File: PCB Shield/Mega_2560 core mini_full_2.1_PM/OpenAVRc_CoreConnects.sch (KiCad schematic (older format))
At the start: 19 parts, among them P1 2560-core, P10 RX1TX1, P16 LCD, P6 Micro_sd, P9 SPI, Q1 IRLML5203

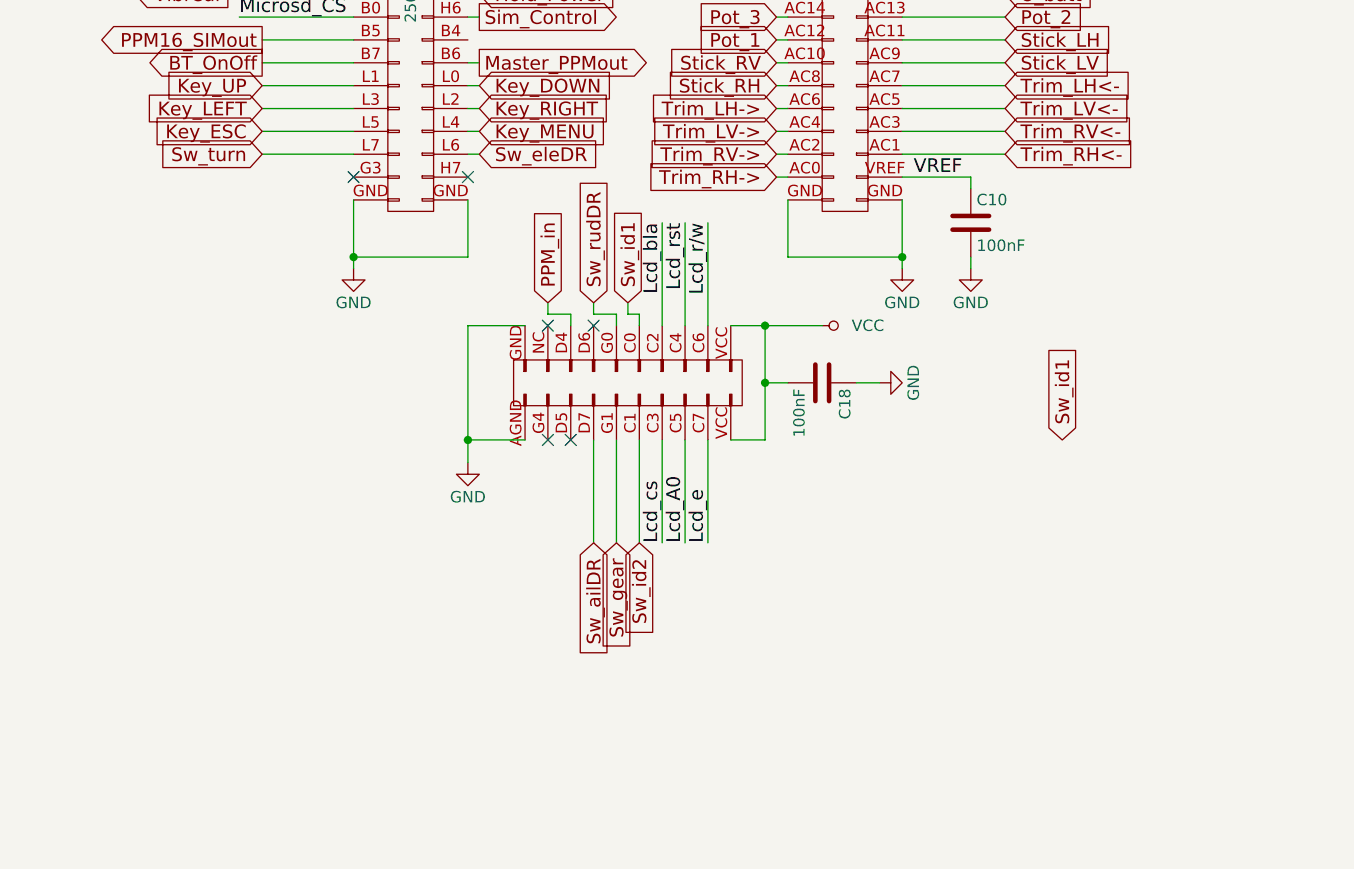
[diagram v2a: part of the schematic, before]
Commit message: Update schematic & pcb files
-remove P27.
-clean hold_power signal.
-add G3,H7 and G4 pins as dummy pins on 3 pins connector.
-update schematic.
-remove package errors in pcbnew.
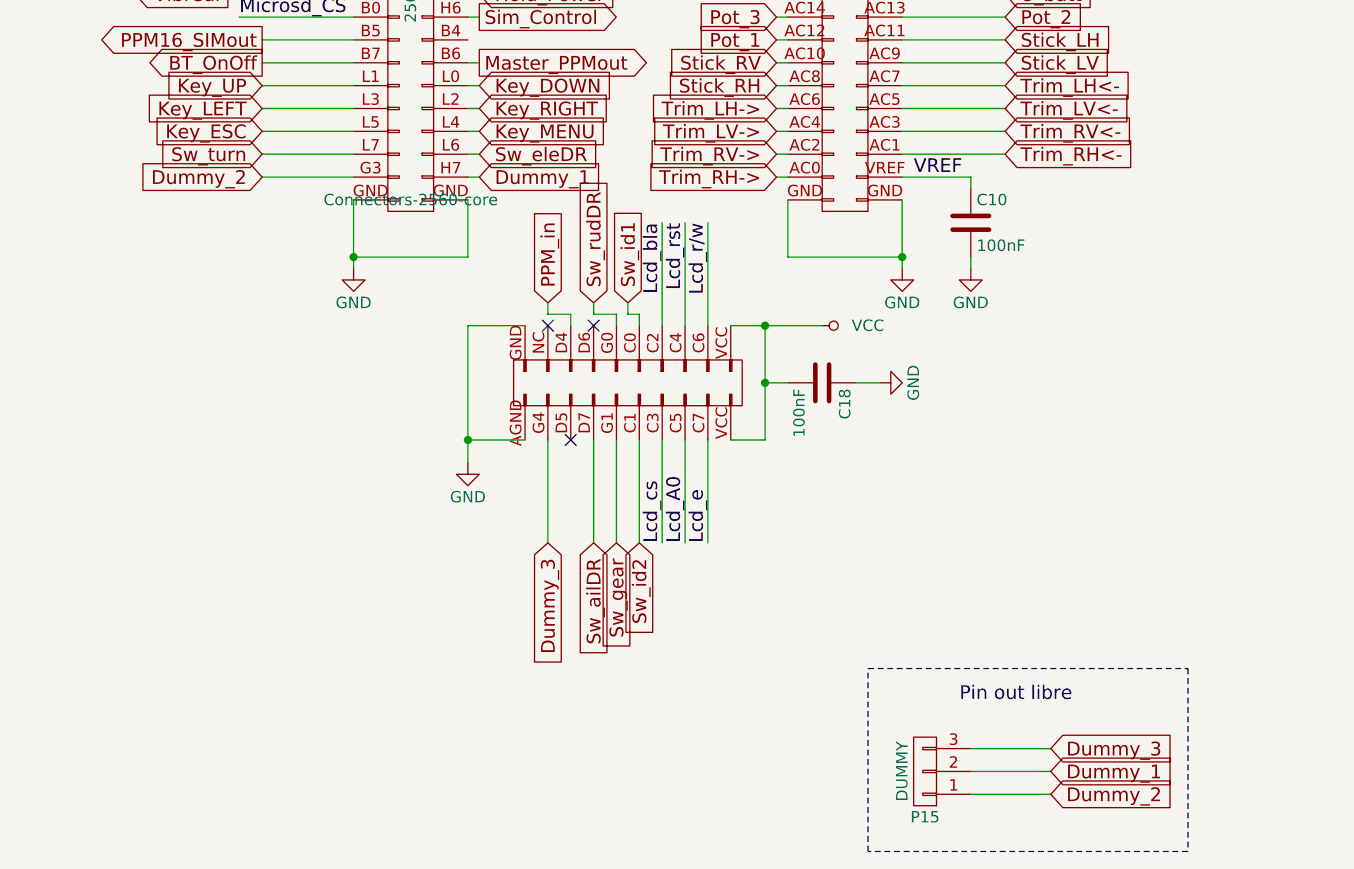
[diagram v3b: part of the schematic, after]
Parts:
- added P15: DUMMY, symbol CONN_01X03
- P1: footprint (none) -> Connectors-2560-core
- Q1: footprint (none) -> SOT-23_MOS_P
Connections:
- net Dummy_2: now reaches P1.G3 (P38)
- net Dummy_2: now also P15.1 (P1)
- net Dummy_3: now reaches P1.G4 (P97)
- net Dummy_3: now also P15.3 (P3)
- net Dummy_1: now reaches P1.H7 (P37)
- net Dummy_1: now also P15.2 (P2)
- no-connect marks 7 -> 4
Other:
- note added: "Pin out libre"

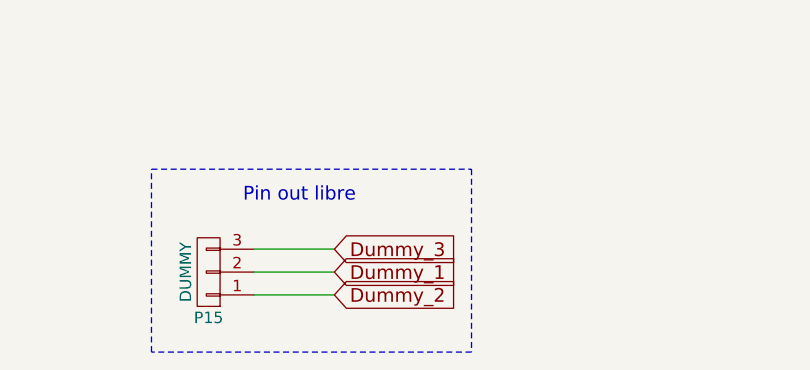
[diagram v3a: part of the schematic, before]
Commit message: Update schematic & pcb files
add mosfet function
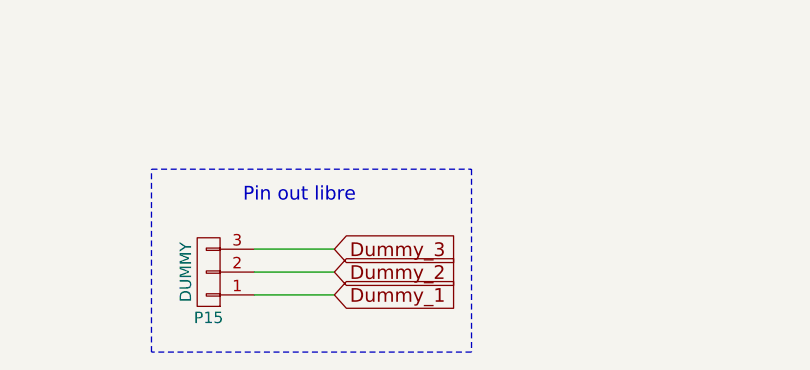
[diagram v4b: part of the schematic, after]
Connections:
- net Dummy_1: now also P15.1 (P1); no longer P15.2 (P2)
- net Dummy_2: now also P15.2 (P2); no longer P15.1 (P1)
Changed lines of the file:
@@
 Sheet 3 7
 Title "Shield Mega2560 core Full"
-Date "2018-03-06"
+Date "2018-03-16"
 Rev "2.10"
 Comp "© Team OpenAVRc"
@@
 	2700 5650 2700 5200
 Text GLabel 4900 6650 2    60   Input ~ 0
+Dummy_2
+Text GLabel 4900 6750 2    60   Input ~ 0
 Dummy_1
-Text GLabel 4900 6750 2    60   Input ~ 0
-Dummy_2
 Text GLabel 4900 6550 2    60   Input ~ 0
 Dummy_3

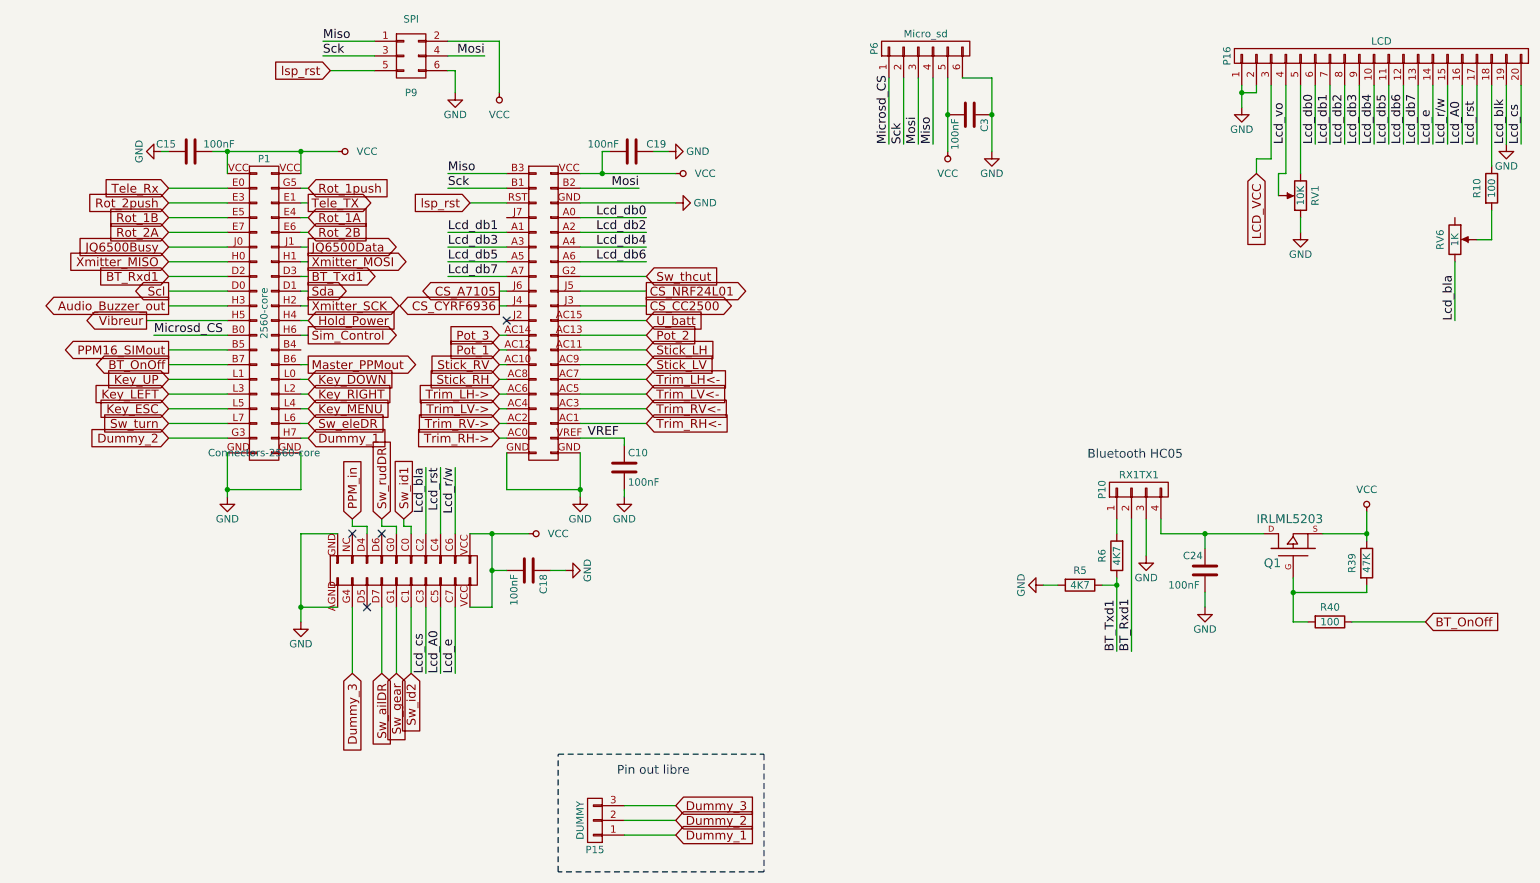
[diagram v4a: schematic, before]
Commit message: Udpade shild v2.1
remove c10 on VREF and R21,R38 on I2C
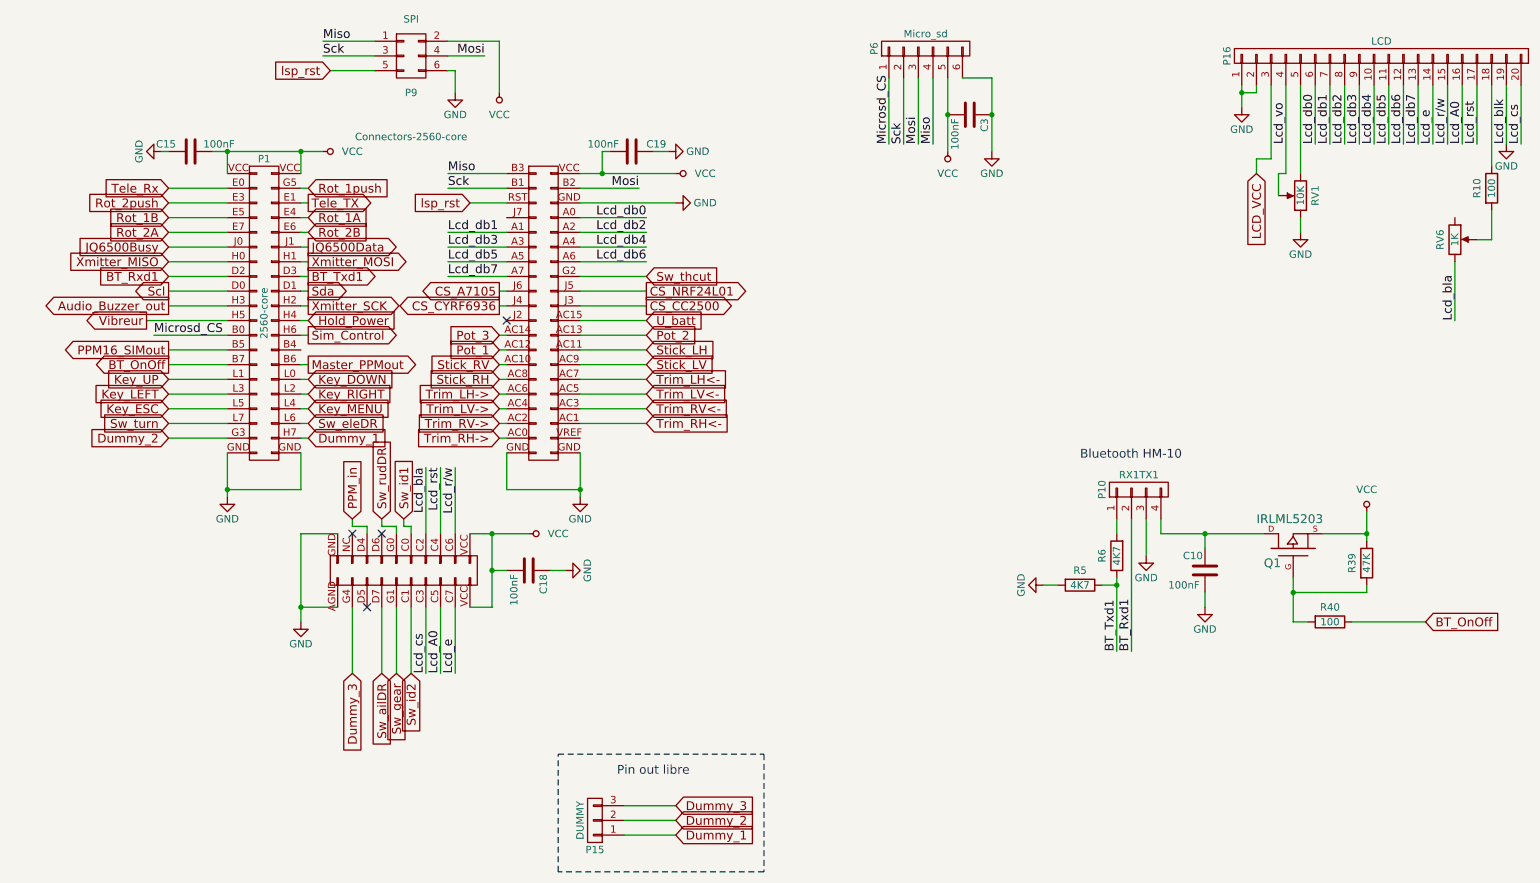
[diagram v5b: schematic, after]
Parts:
- removed C10: 100nF, Capacitors_SMD:C_1206, symbol C-RESCUE-Mega_2560_core_mini_full_2.0
- renumbered C24 to C10
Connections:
- net VREF: no longer names the net of P1.VREF (P44)
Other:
- note added: "Bluetooth HM-10"
- note removed: "Bluetooth HC05"
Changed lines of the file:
@@
 Sheet 3 7
 Title "Shield Mega2560 core Full"
-Date "2018-03-16"
+Date "2018-04-19"
 Rev "2.10"
 Comp "© Team OpenAVRc"
@@
 L VCC #PWR051
 U 1 1 59C5DDE8
-P 2600 2100
-F 0 "#PWR051" H 2600 1950 50  0001 C CNN
-F 1 "VCC" V 2600 2300 50  0000 C CNN
-F 2 "" H 2600 2100 50  0000 C CNN
-F 3 "" H 2600 2100 50  0000 C CNN
-	1    2600 2100
+P 2500 2100
+F 0 "#PWR051" H 2500 1950 50  0001 C CNN
+F 1 "VCC" V 2500 2300 50  0000 C CNN
+F 2 "" H 2500 2100 50  0000 C CNN
+F 3 "" H 2500 2100 50  0000 C CNN
+	1    2500 2100
 	0    1    1    0
 $EndComp
@@
 NoConn ~ 2800 5200
 NoConn ~ 3750 3250
-Text Label 4300 4050 0    60   ~ 0
-VREF
-$Comp
-L C-RESCUE-Mega_2560_core_mini_full_2.0 C10
-U 1 1 59C5DE3E
-P 4550 4250
-F 0 "C10" H 4575 4350 50  0000 L CNN
-F 1 "100nF" H 4575 4150 50  0000 L CNN
-F 2 "Capacitors_SMD:C_1206" H 4588 4100 50  0001 C CNN
-F 3 "" H 4550 4250 50  0000 C CNN
-	1    4550 4250
-	1    0    0    -1
-$EndComp
-$Comp
-L GND-RESCUE-Mega_2560_core_mini_full_2.0 #PWR054
-U 1 1 59C5DE45
-P 4550 4450
-F 0 "#PWR054" H 4550 4200 50  0001 C CNN
-F 1 "GND" H 4550 4300 50  0000 C CNN
-F 2 "" H 4550 4450 50  0000 C CNN
-F 3 "" H 4550 4450 50  0000 C CNN
-	1    4550 4450
-	1    0    0    -1
-$EndComp
 NoConn ~ 2700 4700
 $Comp
@@
 $EndComp
 $Comp
-L GND-RESCUE-Mega_2560_core_mini_full_2.0 #PWR055
+L GND-RESCUE-Mega_2560_core_mini_full_2.0 #PWR054
 U 1 1 59C5DE66
 P 4150 4950
-F 0 "#PWR055" H 4150 4700 50  0001 C CNN
+F 0 "#PWR054" H 4150 4700 50  0001 C CNN
 F 1 "GND" H 4150 4800 50  0000 C CNN
 F 2 "" H 4150 4950 50  0000 C CNN
@@
 $EndComp
 $Comp
-L GND-RESCUE-Mega_2560_core_mini_full_2.0 #PWR056
+L GND-RESCUE-Mega_2560_core_mini_full_2.0 #PWR055
 U 1 1 59C5DE7A
 P 1400 2100
-F 0 "#PWR056" H 1400 1850 50  0001 C CNN
+F 0 "#PWR055" H 1400 1850 50  0001 C CNN
 F 1 "GND" H 1400 1950 50  0000 C CNN
 F 2 "" H 1400 2100 50  0000 C CNN
@@
 $EndComp
 $Comp
-L GND-RESCUE-Mega_2560_core_mini_full_2.0 #PWR057
+L GND-RESCUE-Mega_2560_core_mini_full_2.0 #PWR056
 U 1 1 59C5DE80
 P 4850 2100
-F 0 "#PWR057" H 4850 1850 50  0001 C CNN
+F 0 "#PWR056" H 4850 1850 50  0001 C CNN
 F 1 "GND" V 4850 1900 50  0000 C CNN
 F 2 "" H 4850 2100 50  0000 C CNN
@@
 $EndComp
 $Comp
-L GND-RESCUE-Mega_2560_core_mini_full_2.0 #PWR058
+L GND-RESCUE-Mega_2560_core_mini_full_2.0 #PWR057
 U 1 1 59C5BE4B
 P 7050 2100
-F 0 "#PWR058" H 7050 1850 50  0001 C CNN
+F 0 "#PWR057" H 7050 1850 50  0001 C CNN
 F 1 "GND" H 7050 1950 50  0000 C CNN
 F 2 "" H 7050 2100 50  0000 C CNN
@@
 $EndComp
 $Comp
-L VCC #PWR059
+L VCC #PWR058
 U 1 1 59C5BE51
 P 6750 2100
-F 0 "#PWR059" H 6750 1950 50  0001 C CNN
+F 0 "#PWR058" H 6750 1950 50  0001 C CNN
 F 1 "VCC" H 6750 2250 50  0000 C CNN
 F 2 "" H 6750 2100 50  0000 C CNN
@@
 Miso
 $Comp
-L GND-RESCUE-Mega_2560_core_mini_full_2.0 #PWR060
+L GND-RESCUE-Mega_2560_core_mini_full_2.0 #PWR059
 U 1 1 59C5BE5B
 P 8750 1800
-F 0 "#PWR060" H 8750 1550 50  0001 C CNN
+F 0 "#PWR059" H 8750 1550 50  0001 C CNN
 F 1 "GND" H 8750 1650 50  0000 C CNN
 F 2 "" H 8750 1800 50  0000 C CNN
@@
 Lcd_cs
 $Comp
-L GND-RESCUE-Mega_2560_core_mini_full_2.0 #PWR061
+L GND-RESCUE-Mega_2560_core_mini_full_2.0 #PWR060
 U 1 1 59C5BE7F
 P 10550 2050
-F 0 "#PWR061" H 10550 1800 50  0001 C CNN
+F 0 "#PWR060" H 10550 1800 50  0001 C CNN
 F 1 "GND" H 10550 1900 50  0000 C CNN
 F 2 "" H 10550 2050 50  0000 C CNN
@@
 Lcd_db5
 $Comp
-L GND-RESCUE-Mega_2560_core_mini_full_2.0 #PWR062
+L GND-RESCUE-Mega_2560_core_mini_full_2.0 #PWR061
 U 1 1 59C5BE86
 P 9150 2650
-F 0 "#PWR062" H 9150 2400 50  0001 C CNN
+F 0 "#PWR061" H 9150 2400 50  0001 C CNN
 F 1 "GND" H 9150 2500 50  0000 C CNN
 F 2 "" H 9150 2650 50  0000 C CNN
@@
 $EndComp
 $Comp
-L C-RESCUE-Mega_2560_core_mini_full_2.0 C24
+L C-RESCUE-Mega_2560_core_mini_full_2.0 C10
 U 1 1 59C5BEA1
 P 8500 4950
-F 0 "C24" H 8350 5050 50  0000 L CNN
+F 0 "C10" H 8350 5050 50  0000 L CNN
 F 1 "100nF" H 8250 4850 50  0000 L CNN
 F 2 "Capacitors_SMD:C_1206" H 8538 4800 50  0001 C CNN
@@
 $EndComp
 $Comp
-L GND-RESCUE-Mega_2560_core_mini_full_2.0 #PWR063
+L GND-RESCUE-Mega_2560_core_mini_full_2.0 #PWR062
 U 1 1 59C5BEA8
 P 8100 4850
-F 0 "#PWR063" H 8100 4600 50  0001 C CNN
+F 0 "#PWR062" H 8100 4600 50  0001 C CNN
 F 1 "GND" H 8100 4700 50  0000 C CNN
 F 2 "" H 8100 4850 50  0000 C CNN
@@
 $EndComp
 $Comp
-L GND-RESCUE-Mega_2560_core_mini_full_2.0 #PWR064
+L GND-RESCUE-Mega_2560_core_mini_full_2.0 #PWR063
 U 1 1 59C5BEAE
 P 8500 5200
-F 0 "#PWR064" H 8500 4950 50  0001 C CNN
+F 0 "#PWR063" H 8500 4950 50  0001 C CNN
 F 1 "GND" H 8500 5050 50  0000 C CNN
 F 2 "" H 8500 5200 50  0000 C CNN
@@
 Text Label 7900 5500 1    60   ~ 0
 BT_Txd1
-Text Notes 7700 4200 0    60   ~ 0
-Bluetooth HC05
+Text Notes 7650 4200 0    60   ~ 0
+Bluetooth HM-10
 Text GLabel 1450 2350 0    60   Input ~ 0
 Tele_Rx
@@
 $EndComp
 $Comp
-L VCC #PWR065
+L VCC #PWR064
 U 1 1 59E0DFF9
 P 9600 4550
-F 0 "#PWR065" H 9600 4400 50  0001 C CNN
+F 0 "#PWR064" H 9600 4400 50  0001 C CNN
 F 1 "VCC" H 9600 4700 50  0000 C CNN
 F 2 "" H 9600 4550 50  0000 C CNN
@@
 $EndComp
 $Comp
-L GND-RESCUE-Mega_2560_core_mini_full_2.0 #PWR066
+L GND-RESCUE-Mega_2560_core_mini_full_2.0 #PWR065
 U 1 1 59EF4C7A
 P 7400 5050
-F 0 "#PWR066" H 7400 4800 50  0001 C CNN
+F 0 "#PWR065" H 7400 4800 50  0001 C CNN
 F 1 "GND" H 7400 4900 50  0000 C CNN
 F 2 "" H 7400 5050 50  0000 C CNN
@@
 F 0 "P1" H 2100 4650 50  0000 C CNN
 F 1 "2560-core" V 2100 3600 50  0000 C CNN
-F 2 "Connectors-2560-core" H 2100 2650 50  0000 C CNN
+F 2 "Connectors-2560-core" H 3100 4800 50  0000 C CNN
 F 3 "" H 2100 2650 50  0000 C CNN
 	1    50   3400
@@
 	2350 2350 2400 2350
 Wire Wire Line
-	4550 4050 4250 4050
-Wire Wire Line
 	3500 4700 3900 4700
-Wire Wire Line
-	4550 4400 4550 4450
-Wire Wire Line
-	4550 4100 4550 4050
 Wire Wire Line
 	3750 4400 4250 4400
@@
 	2350 2100 2350 2250
 Wire Wire Line
-	1750 2100 2600 2100
+	1750 2100 2500 2100
 Wire Wire Line
 	1850 2250 1850 2100
